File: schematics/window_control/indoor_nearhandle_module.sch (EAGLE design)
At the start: 19 parts, among them J1 J2, J2 J2, Q1 2N3904, SW1 MRS-101-2C3-B, U1 ESP32, U4 SN74LS32N

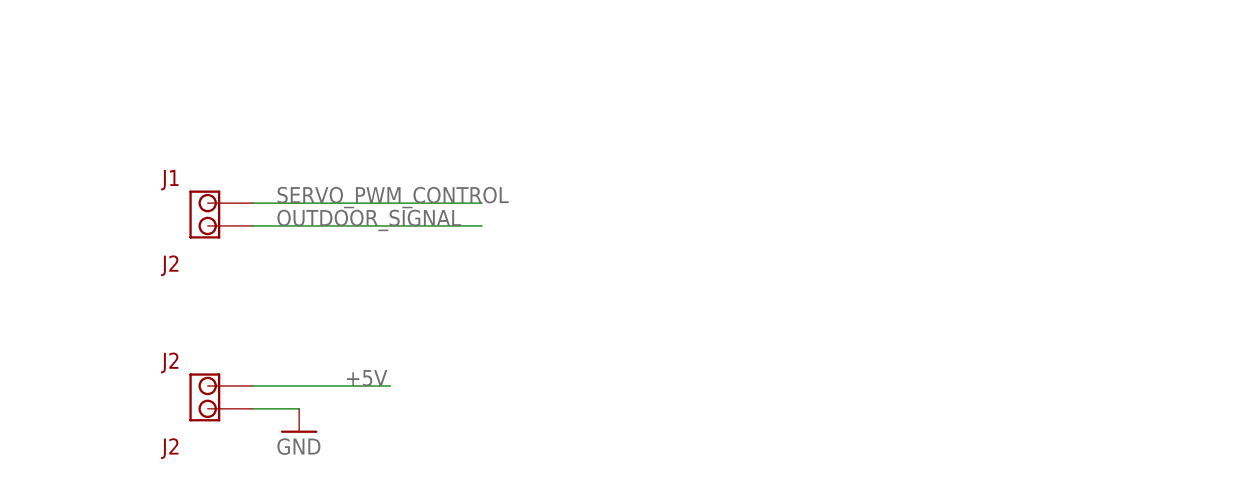
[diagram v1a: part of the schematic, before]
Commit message: Connectors changed
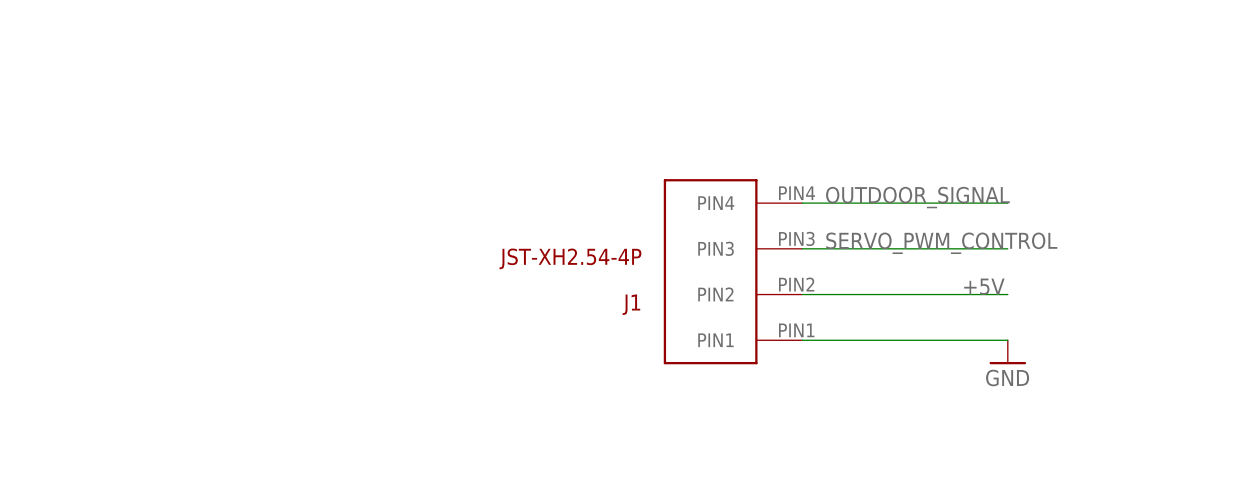
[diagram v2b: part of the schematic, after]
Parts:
- removed J2: J2, my_devices:J2
- J1: value J2 -> JST-XH2.54-4P; device my_devices:J2 -> my_devices:JST-XH254-4P
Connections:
- net +5V: now also J1.PIN2; no longer J2.PIN_1
- net GND: now also J1.PIN1; no longer J2.PIN_2
- net OUTDOOR_SIGNAL: now also J1.PIN4; no longer J1.PIN_2
- net SERVO_PWM_CONTROL: now also J1.PIN3; no longer J1.PIN_1
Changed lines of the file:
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@@
 <part name="SB2" library="my_devices" deviceset="SB-NO" device="" value="FSMRA6JH"/>
 <part name="GND9" library="supply1" library_urn="urn:adsk.eagle:library:371" deviceset="GND" device=""/>
-<part name="J1" library="my_devices" deviceset="J2" device=""/>
-<part name="J2" library="my_devices" deviceset="J2" device=""/>
-<part name="GND1" library="supply1" library_urn="urn:adsk.eagle:library:371" deviceset="GND" device=""/>
 <part name="U1" library="my_devices" deviceset="ESP32" device=""/>
 <part name="GND2" library="supply1" library_urn="urn:adsk.eagle:library:371" deviceset="GND" device=""/>
@@
 <part name="R6" library="my_devices" deviceset="RD" device="" value="5K"/>
 <part name="GND8" library="supply1" library_urn="urn:adsk.eagle:library:371" deviceset="GND" device=""/>
+<part name="J1" library="my_devices" deviceset="JST-XH254-4P" device="" value="JST-XH2.54-4P"/>
+<part name="GND5" library="supply1" library_urn="urn:adsk.eagle:library:371" deviceset="GND" device=""/>
 </parts>
 <sheets>
@@
 <attribute name="VALUE" x="66.04" y="55.88" size="1.778" layer="96"/>
 </instance>
-<instance part="J1" gate="G$1" x="-147.32" y="66.04" smashed="yes" grouprefs="INPUT_CONNECTORS">
-<attribute name="NAME" x="-149.86" y="67.945" size="1.778" layer="94"/>
-<attribute name="VALUE" x="-149.86" y="58.42" size="1.778" layer="94"/>
-</instance>
-<instance part="J2" gate="G$1" x="-147.32" y="45.72" smashed="yes" grouprefs="INPUT_CONNECTORS">
-<attribute name="NAME" x="-149.86" y="47.625" size="1.778" layer="94"/>
-<attribute name="VALUE" x="-149.86" y="38.1" size="1.778" layer="94"/>
-</instance>
-<instance part="GND1" gate="1" x="-134.62" y="40.64" smashed="yes" grouprefs="INPUT_CONNECTORS">
-<attribute name="VALUE" x="-137.16" y="38.1" size="1.778" layer="96"/>
-</instance>
 <instance part="U1" gate="G$1" x="-147.32" y="208.28" smashed="yes" grouprefs="ESP1">
 <attribute name="NAME" x="-152.4" y="236.22" size="1.778" layer="94"/>
@@
 <instance part="GND8" gate="1" x="-104.14" y="177.8" smashed="yes" grouprefs="ESP1">
 <attribute name="VALUE" x="-106.68" y="175.26" size="1.778" layer="96"/>
+</instance>
+<instance part="J1" gate="G$1" x="-83.82" y="58.42" smashed="yes" rot="R180" grouprefs="INPUT_CONNECTORS">
+<attribute name="NAME" x="-96.52" y="55.88" size="1.778" layer="94" rot="R180"/>
+<attribute name="NAME" x="-96.52" y="55.88" size="1.778" layer="94" rot="R180"/>
+<attribute name="VALUE" x="-96.52" y="60.96" size="1.778" layer="94" rot="R180"/>
+</instance>
+<instance part="GND5" gate="1" x="-55.88" y="48.26" smashed="yes" grouprefs="INPUT_CONNECTORS">
+<attribute name="VALUE" x="-58.42" y="45.72" size="1.778" layer="96"/>
 </instance>
 </instances>
@@
 </segment>
 <segment>
-<pinref part="J2" gate="G$1" pin="PIN_1"/>
-<wire x1="-139.7" y1="45.72" x2="-124.46" y2="45.72" width="0.1524" layer="91" grouprefs="INPUT_CONNECTORS"/>
-<label x="-129.54" y="45.72" size="1.778" layer="95" grouprefs="INPUT_CONNECTORS"/>
-</segment>
-<segment>
 <pinref part="U1" gate="G$1" pin="5V"/>
 <wire x1="-167.64" y1="185.42" x2="-193.04" y2="185.42" width="0.1524" layer="91" grouprefs="ESP1"/>
 <label x="-193.04" y="185.42" size="1.778" layer="95" grouprefs="ESP1"/>
+</segment>
+<segment>
+<pinref part="J1" gate="G$1" pin="PIN2"/>
+<wire x1="-78.74" y1="55.88" x2="-55.88" y2="55.88" width="0.1524" layer="91" grouprefs="INPUT_CONNECTORS"/>
+<label x="-60.96" y="55.88" size="1.778" layer="95" grouprefs="INPUT_CONNECTORS"/>
 </segment>
 </net>
@@
 </segment>
 <segment>
-<pinref part="J2" gate="G$1" pin="PIN_2"/>
-<pinref part="GND1" gate="1" pin="GND"/>
-<wire x1="-139.7" y1="43.18" x2="-134.62" y2="43.18" width="0.1524" layer="91" grouprefs="INPUT_CONNECTORS"/>
-</segment>
-<segment>
 <pinref part="U1" gate="G$1" pin="GND"/>
 <wire x1="-127" y1="231.14" x2="-83.82" y2="231.14" width="0.1524" layer="91" grouprefs="ESP1"/>
@@
 <pinref part="R6" gate="G$1" pin="P1"/>
 <pinref part="GND8" gate="1" pin="GND"/>
+</segment>
+<segment>
+<pinref part="J1" gate="G$1" pin="PIN1"/>
+<wire x1="-78.74" y1="50.8" x2="-55.88" y2="50.8" width="0.1524" layer="91" grouprefs="INPUT_CONNECTORS"/>
+<pinref part="GND5" gate="1" pin="GND"/>
 </segment>
 </net>
@@
 </segment>
 <segment>
-<pinref part="J1" gate="G$1" pin="PIN_1"/>
-<wire x1="-139.7" y1="66.04" x2="-114.3" y2="66.04" width="0.1524" layer="91" grouprefs="INPUT_CONNECTORS"/>
-<label x="-137.16" y="66.04" size="1.778" layer="95" grouprefs="INPUT_CONNECTORS"/>
+<pinref part="J1" gate="G$1" pin="PIN3"/>
+<wire x1="-78.74" y1="60.96" x2="-55.88" y2="60.96" width="0.1524" layer="91" grouprefs="INPUT_CONNECTORS"/>
+<label x="-76.2" y="60.96" size="1.778" layer="95" grouprefs="INPUT_CONNECTORS"/>
 </segment>
 </net>
@@
 <net name="OUTDOOR_SIGNAL" class="0">
 <segment>
-<pinref part="J1" gate="G$1" pin="PIN_2"/>
-<wire x1="-139.7" y1="63.5" x2="-114.3" y2="63.5" width="0.1524" layer="91" grouprefs="INPUT_CONNECTORS"/>
-<label x="-137.16" y="63.5" size="1.778" layer="95" grouprefs="INPUT_CONNECTORS"/>
-</segment>
-<segment>
 <label x="-101.6" y="193.04" size="1.778" layer="95" grouprefs="ESP1"/>
 <pinref part="R6" gate="G$1" pin="P2"/>
 <wire x1="-104.14" y1="195.58" x2="-73.66" y2="195.58" width="0.1524" layer="91"/>
 </segment>
-</net>
+<segment>
+<pinref part="J1" gate="G$1" pin="PIN4"/>
+<wire x1="-78.74" y1="66.04" x2="-55.88" y2="66.04" width="0.1524" layer="91" grouprefs="INPUT_CONNECTORS"/>
+<label x="-76.2" y="66.04" size="1.778" layer="95" grouprefs="INPUT_CONNECTORS"/>
+</segment>
+</net>
